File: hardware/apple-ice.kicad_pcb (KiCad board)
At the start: 2 copper layers, 100 x 77.7 mm, 12 parts, among them J1 TO_SP_DRIVE, P1 A2Bus-apple2, U1 ICE40HX1K-TQ144, U10 SN74LVC8T245PW, U2 SN74LVC8T245PW, U3 SN74LVC8T245PW, U4 SN74LVC8T245PW, U5 SN74LVC8T245PW, U6 MCP1703A-3302_SOT223, U7 MCP1703A-1202_SOT223, U8 W25Q16JVSS, U9 SN74LVC8T245PW

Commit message: FPGA programming and power
Reorginize schematic
Add more footprints and symbols

Signed-off-by: Rangel Ivanov <rangelivanov88@gmail.com>
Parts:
- added C1: 1uF, apple-ice:C_0603_1608Metric_Pad1.08x0.95mm_HandSolder, F.Cu at (103.0, 35.6)
- added C10: 0.1uF, apple-ice:C_0603_1608Metric_Pad1.08x0.95mm_HandSolder, F.Cu at (103.0, 45.6)
- added C11: 0.1uF, apple-ice:C_0603_1608Metric_Pad1.08x0.95mm_HandSolder, F.Cu at (116.0, 35.6)
- added C12: 0.1uF, apple-ice:C_0603_1608Metric_Pad1.08x0.95mm_HandSolder, F.Cu at (107.3, 43.1)
- added C13: 0.1uF, apple-ice:C_0603_1608Metric_Pad1.08x0.95mm_HandSolder, F.Cu at (111.7, 40.6)
- added C14: 0.1uF, apple-ice:C_0603_1608Metric_Pad1.08x0.95mm_HandSolder, F.Cu at (116.0, 38.1)
- added C15: 0.1uF, apple-ice:C_0603_1608Metric_Pad1.08x0.95mm_HandSolder, F.Cu at (107.3, 45.6)
- added C16: 0.1uF, apple-ice:C_0603_1608Metric_Pad1.08x0.95mm_HandSolder, F.Cu at (120.4, 35.6)
- added C2: 1uF, apple-ice:C_0603_1608Metric_Pad1.08x0.95mm_HandSolder, F.Cu at (103.0, 38.1)
- added C3: 1uF, apple-ice:C_0603_1608Metric_Pad1.08x0.95mm_HandSolder, F.Cu at (107.3, 35.6)
- added C4: 1uF, apple-ice:C_0603_1608Metric_Pad1.08x0.95mm_HandSolder, F.Cu at (103.0, 40.6)
- added C5: 0.1uF, apple-ice:C_0603_1608Metric_Pad1.08x0.95mm_HandSolder, F.Cu at (107.3, 38.1)
- added C6: 0.1uF, apple-ice:C_0603_1608Metric_Pad1.08x0.95mm_HandSolder, F.Cu at (111.7, 35.6)
- added C7: 0.1uF, apple-ice:C_0603_1608Metric_Pad1.08x0.95mm_HandSolder, F.Cu at (103.0, 43.1)
- added C8: 0.1uF, apple-ice:C_0603_1608Metric_Pad1.08x0.95mm_HandSolder, F.Cu at (107.3, 40.6)
- added C9: 0.1uF, apple-ice:C_0603_1608Metric_Pad1.08x0.95mm_HandSolder, F.Cu at (111.7, 38.1)
- added R1: 22k, apple-ice:R_0603_1608Metric_Pad0.98x0.95mm_HandSolder, F.Cu at (111.7, 43.1)
- added R2: 22k, apple-ice:R_0603_1608Metric_Pad0.98x0.95mm_HandSolder, F.Cu at (116.0, 40.6)
- added R3: 390, apple-ice:R_0603_1608Metric_Pad0.98x0.95mm_HandSolder, F.Cu at (120.4, 38.1)
- added R4: 22k, apple-ice:R_0603_1608Metric_Pad0.98x0.95mm_HandSolder, F.Cu at (111.7, 45.6)
- added R5: 22k, apple-ice:R_0603_1608Metric_Pad0.98x0.95mm_HandSolder, F.Cu at (116.0, 43.1)
- added R6: 22k, apple-ice:R_0603_1608Metric_Pad0.98x0.95mm_HandSolder, F.Cu at (120.4, 40.6)
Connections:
- U10 pad 1: Net-(U10-Pad1) -> +5V
- U10 pad 23: Net-(U10-Pad23) -> /3.3V
- U10 pad 24: Net-(U10-Pad23) -> /3.3V
- U2 pad 1: Net-(U2-Pad1) -> /3.3V
- U2 pad 11: Net-(U2-Pad11) -> GND
- U2 pad 12: Net-(U2-Pad11) -> GND
- U2 pad 13: Net-(U2-Pad11) -> GND
- U2 pad 14: Net-(U2-Pad14) -> GND
- U2 pad 15: Net-(U2-Pad15) -> GND
- U2 pad 16: Net-(U2-Pad16) -> GND
- U2 pad 17: Net-(U2-Pad17) -> GND
- U2 pad 18: Net-(U2-Pad18) -> GND
- U2 pad 19: Net-(U2-Pad19) -> GND
- U2 pad 2: Net-(U2-Pad2) -> GND
- U2 pad 22: Net-(U2-Pad22) -> GND
- U2 pad 23: Net-(U2-Pad23) -> +5V
- U2 pad 24: Net-(U2-Pad23) -> +5V
- U4 pad 1: Net-(U4-Pad1) -> /3.3V
- U4 pad 23: Net-(U4-Pad23) -> +5V
- U4 pad 24: Net-(U4-Pad23) -> +5V
- U5 pad 1: Net-(U5-Pad1) -> /3.3V
- U5 pad 23: Net-(U5-Pad23) -> +5V
- U5 pad 24: Net-(U5-Pad23) -> +5V
- U9 pad 1: Net-(U9-Pad1) -> /3.3V
- U9 pad 23: Net-(U9-Pad23) -> +5V
- U9 pad 24: Net-(U9-Pad23) -> +5V

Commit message: Begin initial placement and routing
Signed-off-by: Rangel Ivanov <rangelivanov88@gmail.com>
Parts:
- removed the R3 at (120.4, 38.1)
- removed the U2 at (167.0, 51.8)
- removed the U5 at (157.4, 93.0)
- removed the U8 at (129.2, 54.6)
- added C11: 1u, apple-ice:C_0603_1608Metric_Pad1.08x0.95mm_HandSolder, F.Cu at (118.6, 85.5)
- added C12: 100n, apple-ice:C_0603_1608Metric_Pad1.08x0.95mm_HandSolder, F.Cu at (102.5, 88.5)
- added C13: 1u, apple-ice:C_0603_1608Metric_Pad1.08x0.95mm_HandSolder, F.Cu at (106.8, 90.2)
- added C16: 100n, apple-ice:C_0603_1608Metric_Pad1.08x0.95mm_HandSolder, F.Cu at (147.1, 45.1)
- added C21: 1u, apple-ice:C_0603_1608Metric_Pad1.08x0.95mm_HandSolder, F.Cu at (118.6, 83.0)
- added C22: 100n, apple-ice:C_0603_1608Metric_Pad1.08x0.95mm_HandSolder, F.Cu at (147.1, 47.6)
- added C23: 1u, apple-ice:C_0603_1608Metric_Pad1.08x0.95mm_HandSolder, F.Cu at (142.8, 45.1)
- added C24: 100n, apple-ice:C_0603_1608Metric_Pad1.08x0.95mm_HandSolder, F.Cu at (119.8, 79.6)
- added C25: 100n, apple-ice:C_0603_1608Metric_Pad1.08x0.95mm_HandSolder, F.Cu at (153.8, 39.1)
- added C26: 100n, apple-ice:C_0603_1608Metric_Pad1.08x0.95mm_HandSolder, F.Cu at (151.5, 45.1)
- added C27: 100n, apple-ice:C_0603_1608Metric_Pad1.08x0.95mm_HandSolder, F.Cu at (153.8, 41.7)
- added C28: 100n, apple-ice:C_0603_1608Metric_Pad1.08x0.95mm_HandSolder, F.Cu at (162.5, 39.1)
- added C29: 1u, apple-ice:C_0603_1608Metric_Pad1.08x0.95mm_HandSolder, F.Cu at (158.2, 39.1)
- added C30: 100n, apple-ice:C_0603_1608Metric_Pad1.08x0.95mm_HandSolder, F.Cu at (111.2, 90.2)
- added C31: 100n, apple-ice:C_0603_1608Metric_Pad1.08x0.95mm_HandSolder, F.Cu at (158.2, 36.6)
- added C32: 100n, apple-ice:C_0603_1608Metric_Pad1.08x0.95mm_HandSolder, F.Cu at (142.8, 47.6)
- added D1: LED, apple-ice:LED_0603_1608Metric, F.Cu at (131.5, 82.2)
- added D2: LED, apple-ice:LED_0603_1608Metric, F.Cu at (160.0, 46.7)
- added D3: LED, apple-ice:LED_0603_1608Metric, F.Cu at (160.0, 49.3)
- added D4: 1N5819, apple-ice:D_SOD-123, F.Cu at (97.4, 89.0)
- added J2: USB_B_Micro, apple-ice:USB_Micro-B_Molex-105017-0001, F.Cu at (190.6, 37.4)
- added J3: SPI_FLASH_PROG, apple-ice:IDC-Header_2x05_P2.54mm_Vertical, F.Cu at (176.9, 60.0)
- added JP1: J_USB_5V, apple-ice:C_0603_1608Metric_Pad1.08x0.95mm_HandSolder, F.Cu at (153.8, 36.6)
- added R1: 390, apple-ice:R_0603_1608Metric_Pad0.98x0.95mm_HandSolder, B.Cu at (159.2, 99.2)
- added R10: 1k5, apple-ice:R_0603_1608Metric_Pad0.98x0.95mm_HandSolder, F.Cu at (155.8, 44.2)
- added R11: 22, apple-ice:R_0603_1608Metric_Pad0.98x0.95mm_HandSolder, F.Cu at (158.2, 41.7)
- added R12: 22, apple-ice:R_0603_1608Metric_Pad0.98x0.95mm_HandSolder, F.Cu at (122.9, 84.6)
- added R13: 10k, apple-ice:R_0603_1608Metric_Pad0.98x0.95mm_HandSolder, F.Cu at (124.1, 79.6)
- added R14: 10k, apple-ice:R_0603_1608Metric_Pad0.98x0.95mm_HandSolder, F.Cu at (128.5, 79.6)
- added R15: 10k, apple-ice:R_0603_1608Metric_Pad0.98x0.95mm_HandSolder, F.Cu at (127.3, 82.1)
- added R16: 10k, apple-ice:R_0603_1608Metric_Pad0.98x0.95mm_HandSolder, F.Cu at (122.9, 82.1)
- added R17: 2k2, apple-ice:R_0603_1608Metric_Pad0.98x0.95mm_HandSolder, F.Cu at (155.8, 46.7)
- added R18: 2k2, apple-ice:R_0603_1608Metric_Pad0.98x0.95mm_HandSolder, F.Cu at (119.9, 88.1)
- added R19: 2k2, apple-ice:R_0603_1608Metric_Pad0.98x0.95mm_HandSolder, F.Cu at (160.2, 44.2)
- added R20: 22, apple-ice:R_0603_1608Metric_Pad0.98x0.95mm_HandSolder, F.Cu at (162.5, 41.7)
- added R21: 10k, apple-ice:R_0603_1608Metric_Pad0.98x0.95mm_HandSolder, F.Cu at (127.3, 84.6)
- added R22: 10k, apple-ice:R_0603_1608Metric_Pad0.98x0.95mm_HandSolder, F.Cu at (125.6, 73.8)
- added R7: 10k, apple-ice:R_0603_1608Metric_Pad0.98x0.95mm_HandSolder, F.Cu at (151.5, 47.6)
- added R8: 10, apple-ice:R_0603_1608Metric_Pad0.98x0.95mm_HandSolder, F.Cu at (162.5, 36.6)
- added R9: 10, apple-ice:R_0603_1608Metric_Pad0.98x0.95mm_HandSolder, F.Cu at (115.5, 90.2)
- added SW1: SW_Push, apple-ice:SW_SPST_B3S-1000, F.Cu at (146.1, 39.6)
- added SW2: SW_Push, apple-ice:SW_SPST_B3S-1000, F.Cu at (134.8, 50.8)
- added SW3: SW_Push, apple-ice:SW_SPST_B3S-1000, F.Cu at (119.9, 49.6)
- added U10: W25Q16JVSS, apple-ice:SOIC-8_5.23x5.23mm_P1.27mm, F.Cu at (166.1, 59.2)
- added U3: SN74LVC8T245PW, apple-ice:TSSOP-24_4.4x7.8mm_P0.65mm, F.Cu at (139.5, 93.0)
- added U7: SN74LVC8T245PW, apple-ice:TSSOP-24_4.4x7.8mm_P0.65mm, F.Cu at (165.1, 70.4)
- added X1: ECS-2520MV-xxx-xx, apple-ice:Oscillator_SMD_ECS_2520MV-xxx-xx-4Pin_2.5x2.0mm, F.Cu at (124.0, 88.0)
- U2: renamed from U9; moved to B.Cu
- U5: renamed from U3; moved to B.Cu
- moved U2 29.3 mm to (151.5, 93.0)
- moved J1 18.4 mm to (163.3, 82.3)
- moved U1 5.90 mm to (163.5, 93.0)
- moved U5 5.50 mm to (139.5, 93.0)
- moved U4 4.90 mm to (151.5, 93.0)
- renumbered C5 to C1, C6 to C10, C1 to C14, C2 to C15, C15 to C17, C16 to C18, C3 to C19, C9 to C2, C4 to C20, C7 to C3, C10 to C4, C11 to C5, C8 to C6, C12 to C7, C13 to C8, C14 to C9, R4 to R2, R2 to R3, R1 to R4, U10 to U1, U1 to U6, U6 to U8, U7 to U9
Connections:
- net Net-(P1-Pad01) renamed /~IOSEL
- net Net-(P1-Pad20) renamed /~IOSTROBE
- net Net-(P1-Pad31) renamed /~RES
- net Net-(P1-Pad36) renamed /7M
- net Net-(P1-Pad40) renamed /PHI0
- net Net-(P1-Pad41) renamed /~DEVSEL
- C10 pad 2: /3.3V -> +3.3V
- C18 pad 2: /3.3V -> +3.3V
- C19 pad 1: /3.3V -> +3.3V
- C20 pad 1: /1.2V -> +1V2
- C6 pad 2: /3.3V -> +3.3V
- C7 pad 2: /3.3V -> +3.3V
- C8 pad 2: /3.3V -> +3.3V
- C9 pad 2: /3.3V -> +3.3V
- J1 pad 13: /12V -> +12V
- J1 pad 15: /12V -> +12V
- J1 pad 9: /-12V -> -12V
- P1 pad 26: Net-(P1-Pad26) -> GND
- P1 pad 33: Net-(P1-Pad33) -> -12V
- P1 pad 37: Net-(P1-Pad37) -> /Q3
- P1 pad 50: Net-(P1-Pad50) -> +12V
- R2 pad 1: /3.3V -> +3.3V
- R3 pad 1: /3.3V -> +3.3V
- R3 pad 2: Net-(R2-Pad2) (its old number) -> Net-(R3-Pad2)
- R4 pad 1: /3.3V -> +3.3V
- U1 pad 1: +5V -> +3.3V
- U1 pad 18: Net-(P1-Pad21) -> Net-(P1-Pad29)
- U1 pad 19: Net-(P1-Pad32) -> Net-(P1-Pad30)
- U1 pad 20: Net-(P1-Pad30) -> Net-(P1-Pad32)
- U1 pad 21: Net-(P1-Pad29) -> Net-(P1-Pad21)
- U1 pad 22: Net-(R2-Pad2) (its old number) -> Net-(R3-Pad2)
- U1 pad 23: /3.3V -> +5V
- U1 pad 24: /3.3V -> +5V
- U1 pad 3: /~NMI -> /~RDY
- U1 pad 4: /~IRQ -> /~INH
- U1 pad 5: /~INH -> /~IRQ
- U1 pad 6: /~RDY -> /~NMI
- U2 pad 1: /3.3V -> +3.3V
- U2 pad 10: Net-(U1-Pad52) -> /7M_33
- U2 pad 3: Net-(U1-Pad43) -> /RW_33
- U2 pad 4: Net-(U1-Pad44) -> /~IOSEL_33
- U2 pad 5: Net-(U1-Pad45) -> /~IOSTROBE_33
- U2 pad 6: Net-(U1-Pad47) -> /~DEVSEL_33
- U2 pad 7: Net-(U1-Pad48) -> /~RES_33
- U2 pad 8: Net-(U1-Pad49) -> /PHI0_33
- U2 pad 9: Net-(U1-Pad50) -> /Q3_33
- U4 pad 1: /3.3V -> +3.3V
- U4 pad 10: /A0_33 -> /A8_33
- U4 pad 14: /A0 -> /A8
- U4 pad 15: /A1 -> /A9
- U4 pad 16: /A2 -> /A10
- U4 pad 17: /A3 -> /A11
- U4 pad 18: /A4 -> /A12
- U4 pad 19: /A5 -> /A13
- U4 pad 20: /A6 -> /A14
- U4 pad 21: /A7 -> /A15
- U4 pad 3: /A7_33 -> /A15_33
- U4 pad 4: /A6_33 -> /A14_33
- U4 pad 5: /A5_33 -> /A13_33
- U4 pad 6: /A4_33 -> /A12_33
- U4 pad 7: /A3_33 -> /A11_33
- U4 pad 8: /A2_33 -> /A10_33
- U4 pad 9: /A1_33 -> /A9_33
- U5 pad 1: /3.3V -> +3.3V
- U5 pad 10: /D0_33 -> /D7_33
- U5 pad 14: /D0 -> /D7
- U5 pad 15: /D1 -> /D6
- U5 pad 16: /D2 -> /D5
- U5 pad 17: /D3 -> /D4
- U5 pad 18: /D4 -> /D3
- U5 pad 19: /D5 -> /D2
- U5 pad 20: /D6 -> /D1
- U5 pad 21: /D7 -> /D0
- U5 pad 3: /D7_33 -> /D0_33
- U5 pad 4: /D6_33 -> /D1_33
- U5 pad 5: /D5_33 -> /D2_33
- U5 pad 6: /D4_33 -> /D3_33
- U5 pad 7: /D3_33 -> /D4_33
- U5 pad 8: /D2_33 -> /D5_33
- U5 pad 9: /D1_33 -> /D6_33
- U6 pad 100: Net-(U1-Pad100) -> +3.3V
- U6 pad 103: Net-(U1-Pad103) -> GND
- U6 pad 111: Net-(U1-Pad111) -> +1V2
- U6 pad 123: Net-(U1-Pad123) -> +3.3V
- U6 pad 13: Net-(U1-Pad103) -> GND
- U6 pad 132: Net-(U1-Pad103) -> GND
- U6 pad 133: Net-(U1-Pad123) -> +3.3V
- U6 pad 14: Net-(U1-Pad103) -> GND
- U6 pad 140: Net-(U1-Pad103) -> GND
- U6 pad 27: Net-(U1-Pad111) -> +1V2
- U6 pad 30: Net-(U1-Pad30) -> +3.3V
- U6 pad 36: Net-(U1-Pad36) -> +1V2
- U6 pad 37: Net-(R2-Pad2) (its old number) -> /~RDY
- U6 pad 38: /~RDY -> /~INH
- U6 pad 39: /~INH -> /~IRQ
- U6 pad 41: /~IRQ -> /~NMI
- U6 pad 42: /~NMI -> Net-(R3-Pad2)
- U6 pad 43: Net-(U1-Pad43) -> /7M_33
- U6 pad 44: Net-(U1-Pad44) -> /Q3_33
- U6 pad 45: Net-(U1-Pad45) -> /PHI0_33
- U6 pad 46: Net-(U1-Pad46) -> +3.3V
- U6 pad 47: Net-(U1-Pad47) -> /~RES_33
- U6 pad 48: Net-(U1-Pad48) -> /~DEVSEL_33
- U6 pad 49: Net-(U1-Pad49) -> /~IOSTROBE_33
- U6 pad 5: Net-(U1-Pad103) -> GND
- U6 pad 50: Net-(U1-Pad50) -> /~IOSEL_33
- U6 pad 51: Net-(U1-Pad111) -> +1V2
- U6 pad 52: Net-(U1-Pad52) -> /RW_33
- U6 pad 57: Net-(U1-Pad46) -> +3.3V
- U6 pad 59: Net-(U1-Pad103) -> GND
- U6 pad 6: Net-(U1-Pad30) -> +3.3V
- U6 pad 65: Net-(U1-Pad65) -> /iCE40_CDONE
- U6 pad 66: Net-(U1-Pad66) -> /~iCE40_CRESET
- U6 pad 67: Net-(U1-Pad67) -> /iC40_SDO
- U6 pad 68: Net-(U1-Pad68) -> /iC40_SDI
- U6 pad 69: Net-(U1-Pad103) -> GND
- U6 pad 70: Net-(U1-Pad70) -> /iCE40_SCK
- U6 pad 71: Net-(U1-Pad71) -> /~iCE40_CS
- U6 pad 72: Net-(U1-Pad72) -> +3.3V
- U6 pad 78: Net-(U1-Pad78) -> /~FLASH_WP(~IO3)
- U6 pad 79: Net-(U1-Pad79) -> /~FLASH_HOLD(~IO4)
- U6 pad 80: Net-(U1-Pad80) -> /BTN1
- U6 pad 81: Net-(U1-Pad81) -> /BTN2
- U6 pad 86: Net-(U1-Pad103) -> GND
- U6 pad 87: Net-(U1-Pad87) -> /LED1
- U6 pad 88: Net-(U1-Pad88) -> /LED2
- U6 pad 89: Net-(U1-Pad100) -> +3.3V
- U6 pad 90: Net-(U1-Pad90) -> /USB_P
- U6 pad 91: Net-(U1-Pad91) -> /USB_N
- U6 pad 92: Net-(U1-Pad111) -> +1V2
- U6 pad 93: Net-(U1-Pad93) -> /16Mhz
- U6 pad 95: Net-(U1-Pad95) -> /USB_PU
- U8 pad 3: /3.3V -> +3.3V
- U9 pad 3: /1.2V -> +1V2
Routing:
- net /RW: track 0.00 -> 52.0 mm, vias 0 -> 1
- net /~IOSTROBE: track 0.00 -> 35.1 mm, vias 0 -> 1
- net /~RES: track 0.00 -> 32.0 mm
- net /~IOSEL: track 0.00 -> 31.9 mm, vias 0 -> 1
- net Net-(P1-Pad29): track 0.00 -> 30.9 mm, vias 0 -> 1
- net Net-(P1-Pad30): track 0.00 -> 28.6 mm, vias 0 -> 1
- net /RW_33: track 0.00 -> 23.4 mm, vias 0 -> 1
- net Net-(P1-Pad32): track 0.00 -> 22.9 mm, vias 0 -> 1
- net /~IOSEL_33: track 0.00 -> 22.2 mm, vias 0 -> 1
- net /A15: track 0.00 -> 22.0 mm
- net /~IOSTROBE_33: track 0.00 -> 20.9 mm, vias 0 -> 1
- net /A14: track 0.00 -> 20.4 mm
- net /~DEVSEL_33: track 0.00 -> 19.9 mm, vias 0 -> 1
- net /~RES_33: track 0.00 -> 18.8 mm, vias 0 -> 1
- net /A13: track 0.00 -> 18.6 mm
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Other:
- net class Default: trace_width 0.25 -> 0.2; via_dia 0.8 -> 0.7

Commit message: Initial placement V2
Signed-off-by: Rangel Ivanov <rangelivanov88@gmail.com>
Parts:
- C1, C10, C2, C7, R4: moved to B.Cu
- moved C14 104.4 mm to (188.6, 95.2), turned to 90 degrees
- moved C19 98.6 mm to (188.6, 91.4), turned to 270 degrees
- moved C15 97.6 mm to (188.6, 84.9), turned to 90 degrees
- moved C20 94.8 mm to (188.6, 81.3), turned to 270 degrees
- moved J2 94.7 mm to (95.9, 36.7), turned to 270 degrees
- moved U8 87.7 mm to (182.9, 93.6), turned to 180 degrees
- moved C3 85.1 mm to (169.7, 96.0), turned to 180 degrees
- moved C6 79.7 mm to (169.7, 90.2), turned to 180 degrees
- moved U9 76.8 mm to (182.9, 83.4), turned to 180 degrees
- moved C5 73.3 mm to (157.5, 96.0), turned to 180 degrees
- moved R3 72.6 mm to (171.7, 87.1)
- moved R2 69.9 mm to (167.9, 87.1), turned to 180 degrees
- moved C2 67.1 mm to (145.5, 96.0)
- moved C9 66.6 mm to (157.5, 90.2), turned to 180 degrees
- moved C4 65.9 mm to (145.4, 96.0), turned to 180 degrees
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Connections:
- U6 pad 112: Net-(U6-Pad112) -> /PH0
- U6 pad 113: Net-(U6-Pad113) -> /PH1
- U6 pad 114: Net-(U6-Pad114) -> /PH2
- U6 pad 115: Net-(U6-Pad115) -> /PH3
- U6 pad 116: Net-(U6-Pad116) -> /~WREQ
- U6 pad 117: Net-(U6-Pad117) -> /SEL
- U6 pad 118: Net-(U6-Pad118) -> /~ENABLE
- U6 pad 119: Net-(U6-Pad119) -> /WRDATA
- U6 pad 120: Net-(U6-Pad120) -> /RDDATA_33
- U6 pad 121: Net-(U6-Pad121) -> /SENSE_33
- U6 pad 58: /PH0 -> Net-(U6-Pad58)
- U6 pad 60: /PH1 -> Net-(U6-Pad60)
- U6 pad 61: /PH2 -> Net-(U6-Pad61)
- U6 pad 62: /PH3 -> Net-(U6-Pad62)
- U6 pad 63: /~WREQ -> Net-(U6-Pad63)
- U6 pad 64: /SEL -> Net-(U6-Pad64)
- U6 pad 73: /~ENABLE -> Net-(U6-Pad73)
- U6 pad 74: /WRDATA -> Net-(U6-Pad74)
- U6 pad 75: /RDDATA_33 -> Net-(U6-Pad75)
- U6 pad 76: /SENSE_33 -> Net-(U6-Pad76)
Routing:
- net /RW: track 52.0 -> 0.00 mm, vias 1 -> 0
- net /~IOSTROBE: track 35.1 -> 0.66 mm, vias 1 -> 0
- net /~RES: track 32.0 -> 0.00 mm
- net /~IOSEL: track 31.9 -> 0.00 mm, vias 1 -> 0
- net Net-(P1-Pad29): track 30.9 -> 0.00 mm, vias 1 -> 0
- net +5V: track 0.00 -> 28.8 mm
- net Net-(P1-Pad30): track 28.6 -> 0.00 mm, vias 1 -> 0
- net /RW_33: track 23.4 -> 0.00 mm, vias 1 -> 0
- net Net-(P1-Pad32): track 22.9 -> 0.00 mm, vias 1 -> 0
- net /~IOSEL_33: track 22.2 -> 0.00 mm, vias 1 -> 0
- net /A15: track 22.0 -> 0.00 mm
- net /~IOSTROBE_33: track 20.9 -> 0.00 mm, vias 1 -> 0
- net /A14: track 20.4 -> 0.00 mm
- net /~DEVSEL_33: track 19.9 -> 0.00 mm, vias 1 -> 0
- net /~RES_33: track 18.8 -> 0.00 mm, vias 1 -> 0
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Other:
- outline, holes or cut-outs redrawn

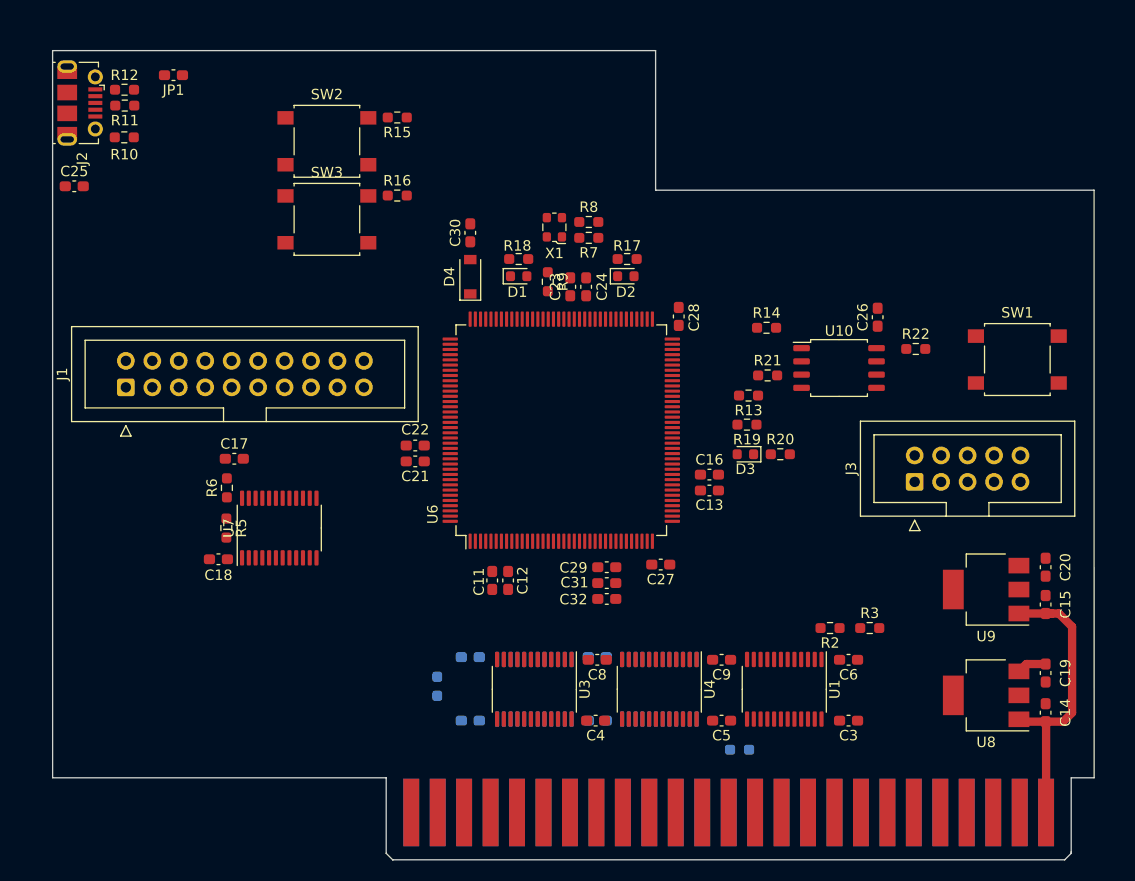
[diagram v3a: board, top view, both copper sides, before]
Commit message: Add new micro USB footprint
Signed-off-by: Rangel Ivanov <rangelivanov88@gmail.com>
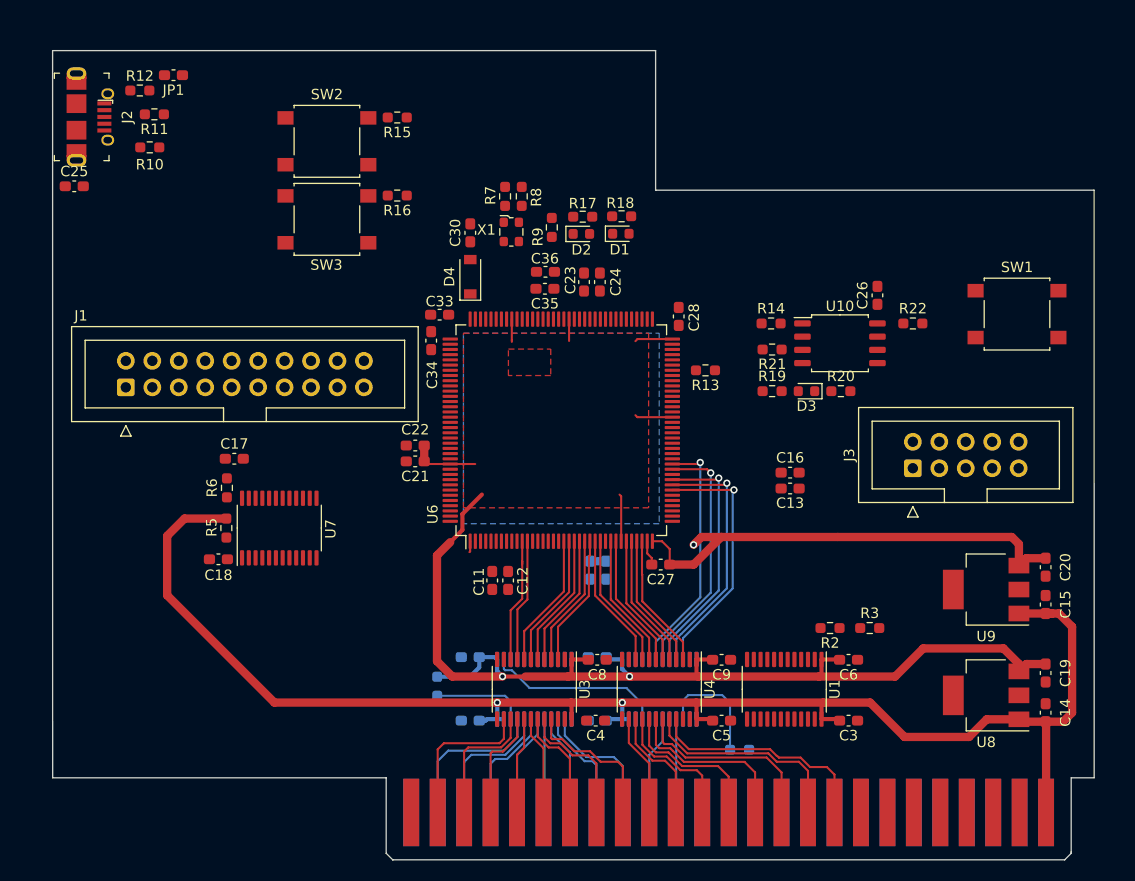
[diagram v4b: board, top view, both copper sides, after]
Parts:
- removed C32: 100n, apple-ice:C_0603_1608Metric_Pad1.08x0.95mm_HandSolder
- added C33: 1u, apple-ice:C_0603_1608Metric_Pad1.08x0.95mm_HandSolder, F.Cu at (130.4, 57.0)
- added C34: 1u, apple-ice:C_0603_1608Metric_Pad1.08x0.95mm_HandSolder, F.Cu at (129.6, 59.5)
- added C35: 100n, apple-ice:C_0603_1608Metric_Pad1.08x0.95mm_HandSolder, F.Cu at (140.5, 54.5)
- added C36: 100n, apple-ice:C_0603_1608Metric_Pad1.08x0.95mm_HandSolder, F.Cu at (140.6, 52.9)
- C29, C31: moved to B.Cu
- J2: footprint apple-ice:USB_Micro-B_Molex-105017-0001 -> apple-ice:MOLEX-0475890001
- moved R18 10.7 mm to (147.9, 47.6)
- moved D1 10.6 mm to (147.8, 49.3)
- moved R7 8.97 mm to (136.7, 45.7), turned to 270 degrees
- moved D3 8.43 mm to (165.6, 64.4)
- moved R20 8.40 mm to (168.9, 64.4)
- moved C13 7.75 mm to (164.1, 73.7)
- moved C16 7.75 mm to (164.1, 72.2)
- moved R8 6.89 mm to (138.3, 45.7), turned to 270 degrees
- moved D2 5.89 mm to (144.0, 49.3)
- moved R17 5.89 mm to (144.1, 47.6)
- moved R9 5.23 mm to (141.2, 48.7), turned to 90 degrees
- moved R13 4.79 mm to (155.9, 62.4)
- moved SW1 4.36 mm to (185.8, 57.0)
- moved X1 4.16 mm to (137.3, 49.1), turned to 0 degrees
- moved R19 4.02 mm to (162.3, 64.4), turned to 0 degrees
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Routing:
- net +3.3V: track 2.86 -> 125.0 mm, vias 0 -> 2
- net +5V: track 28.8 -> 145.1 mm, vias 0 -> 2
- net +1V2: track 0.00 -> 47.8 mm, vias 0 -> 1
- net /Q3_33: track 0.00 -> 24.2 mm, vias 0 -> 1
- net /7M_33: track 0.00 -> 24.2 mm, vias 0 -> 1
- net /PHI0_33: track 0.00 -> 24.0 mm, vias 0 -> 1
- net /~RES_33: track 0.00 -> 23.7 mm, vias 0 -> 1
- net /~DEVSEL_33: track 0.00 -> 23.4 mm, vias 0 -> 1
- net /A15: track 0.00 -> 22.0 mm
- net /A14: track 0.00 -> 20.3 mm
- net /A13: track 0.00 -> 18.7 mm
- net /RW: track 0.00 -> 17.1 mm
- net /A12: track 0.00 -> 16.9 mm
- net /D0: track 0.00 -> 15.3 mm
- net /A11: track 0.00 -> 14.9 mm
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- added copper zone on B.Cu, net +1V2
- added copper zone on F.Cu, net +3.3V

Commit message: More schematic tweaking for easier routing
Signed-off-by: Rangel Ivanov <rangelivanov88@gmail.com>
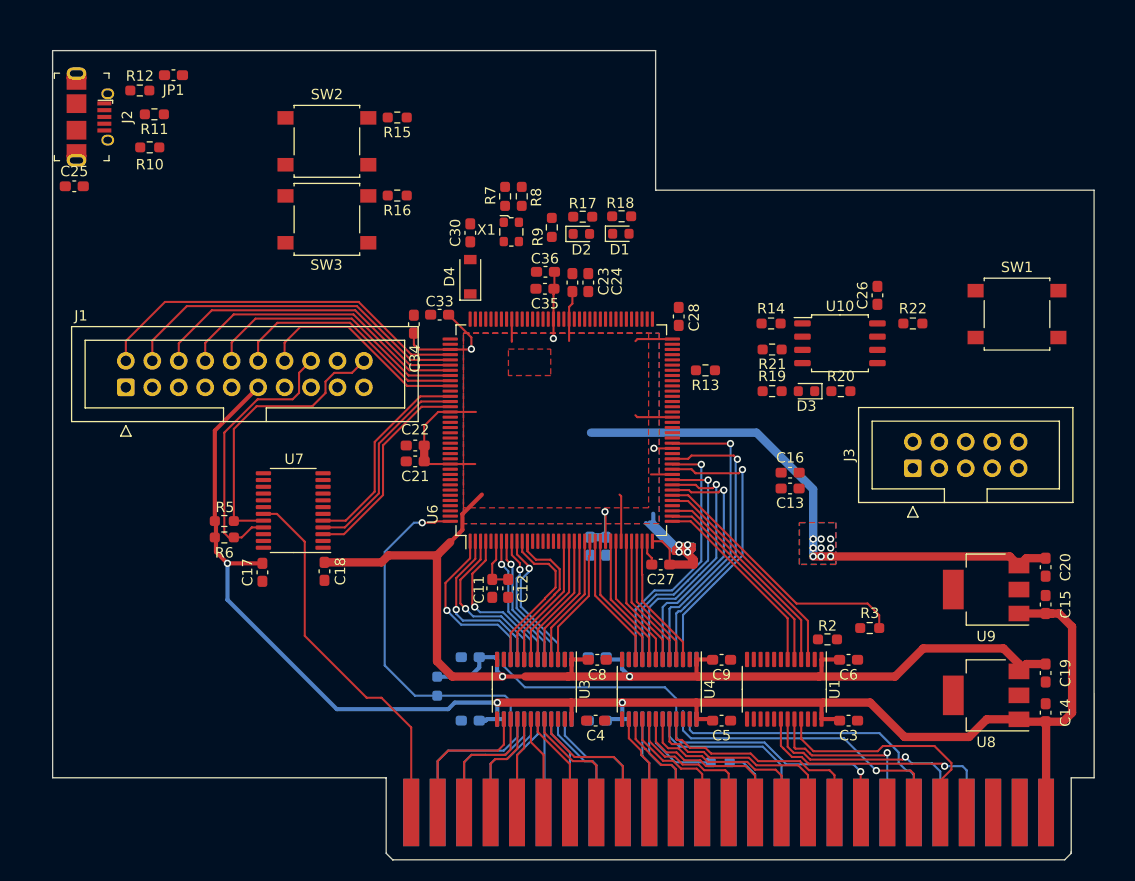
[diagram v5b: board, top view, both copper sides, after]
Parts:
- moved C17 11.2 mm to (113.4, 81.8), turned to 90 degrees
- moved C18 10.2 mm to (119.3, 81.7), turned to 90 degrees
- moved R6 4.77 mm to (109.7, 78.4), turned to 0 degrees
- moved C29 2.30 mm to (144.9, 79.3)
- moved C31 2.30 mm to (146.4, 79.3)
- moved C34 2.29 mm to (127.9, 57.9)
- moved R1 2.22 mm to (157.3, 100.0)
- moved U7 2.15 mm to (116.4, 75.8), turned to 180 degrees
- moved C23 1.12 mm to (143.2, 53.9)
- moved C24 1.12 mm to (144.7, 53.9)
- moved R2 1.12 mm to (167.6, 88.2)
- moved C11 0.76 mm to (135.5, 83.3)
- moved C12 0.76 mm to (137.0, 83.3)
- moved R5 0.70 mm to (109.7, 76.8), turned to 0 degrees
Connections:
- P1 pad 37: /Q3 -> Net-(P1-Pad37)
- R1 pad 1: Net-(R1-Pad1) -> /Q3
- R1 pad 2: /Q3 -> Net-(P1-Pad37)
- U2 pad 10: /7M_33 -> /~RES_33
- U2 pad 14: /7M -> /~RES
- U2 pad 15: Net-(R1-Pad1) -> /~IOSTROBE
- U2 pad 16: /PHI0 -> /RW
- U2 pad 17: /~RES -> /7M
- U2 pad 18: /~DEVSEL -> Net-(U2-Pad18)
- U2 pad 19: /~IOSTROBE -> /Q3
- U2 pad 20: /~IOSEL -> /PHI0
- U2 pad 21: /RW -> /~DEVSEL
- U2 pad 3: /RW_33 -> /~DEVSEL_33
- U2 pad 4: /~IOSEL_33 -> /PHI0_33
- U2 pad 5: /~IOSTROBE_33 -> /Q3_33
- U2 pad 6: /~DEVSEL_33 -> Net-(U2-Pad6)
- U2 pad 7: /~RES_33 -> /7M_33
- U2 pad 8: /PHI0_33 -> /RW_33
- U2 pad 9: /Q3_33 -> /~IOSTROBE_33
- U6 pad 120: /RDDATA_33 -> /~IOSEL_33
- U6 pad 122: Net-(U6-Pad122) -> /RDDATA_33
- U6 pad 144: Net-(U6-Pad144) -> /~D_OE
- U6 pad 37: /~RDY -> /~NMI
- U6 pad 38: /~INH -> /~IRQ
- U6 pad 39: /~IRQ -> /~INH
- U6 pad 41: /~NMI -> /~RDY
- U6 pad 50: /~IOSEL_33 -> Net-(U6-Pad50)
- U6 pad 56: /~D_OE -> Net-(U6-Pad56)
- U7 pad 19: GND -> /~IOSEL
- U7 pad 5: Net-(U7-Pad5) -> /~IOSEL_33
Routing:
- net +1V2: track 47.8 -> 114.9 mm, vias 1 -> 17
- net /PH0: track 0.00 -> 36.7 mm
- net /~IOSEL: track 0.00 -> 36.1 mm
- net /PH1: track 0.00 -> 34.1 mm
- net /PH2: track 0.00 -> 31.2 mm
- net /RW_33: track 0.01 -> 29.2 mm, vias 0 -> 1
- net /~IOSTROBE: track 0.66 -> 29.4 mm, vias 0 -> 1
- net +3.3V: track 125.0 -> 153.7 mm
- net /PH3: track 0.00 -> 28.6 mm
- net /~RES: track 0.00 -> 28.5 mm
- net /~IOSTROBE_33: track 0.00 -> 28.3 mm, vias 0 -> 1
- net /RW: track 17.1 -> 45.2 mm, vias 0 -> 1
- net /SENSE: track 0.00 -> 27.5 mm
- net /RDDATA: track 0.00 -> 26.3 mm
- net /~WREQ: track 0.00 -> 26.0 mm
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- added copper zone on F.Cu, net +1V2
